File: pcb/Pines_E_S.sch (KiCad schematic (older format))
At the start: 27 parts, among them P1 CONN_01X04, P10 CONN_01X02, P11 CONN_01X02, P12 CONN_01X02, P13 CONN_01X02, P14 USB_MINI, P15 CONN_01X02, P16 CONN_02X03, P2 CONN_01X04, P3 CONN_01X03, P4 CONN_01X03, P5 CONN_01X03, P6 CONN_01X03, P7 CONN_01X03, P8 CONN_01X03, P9 CONN_01X02

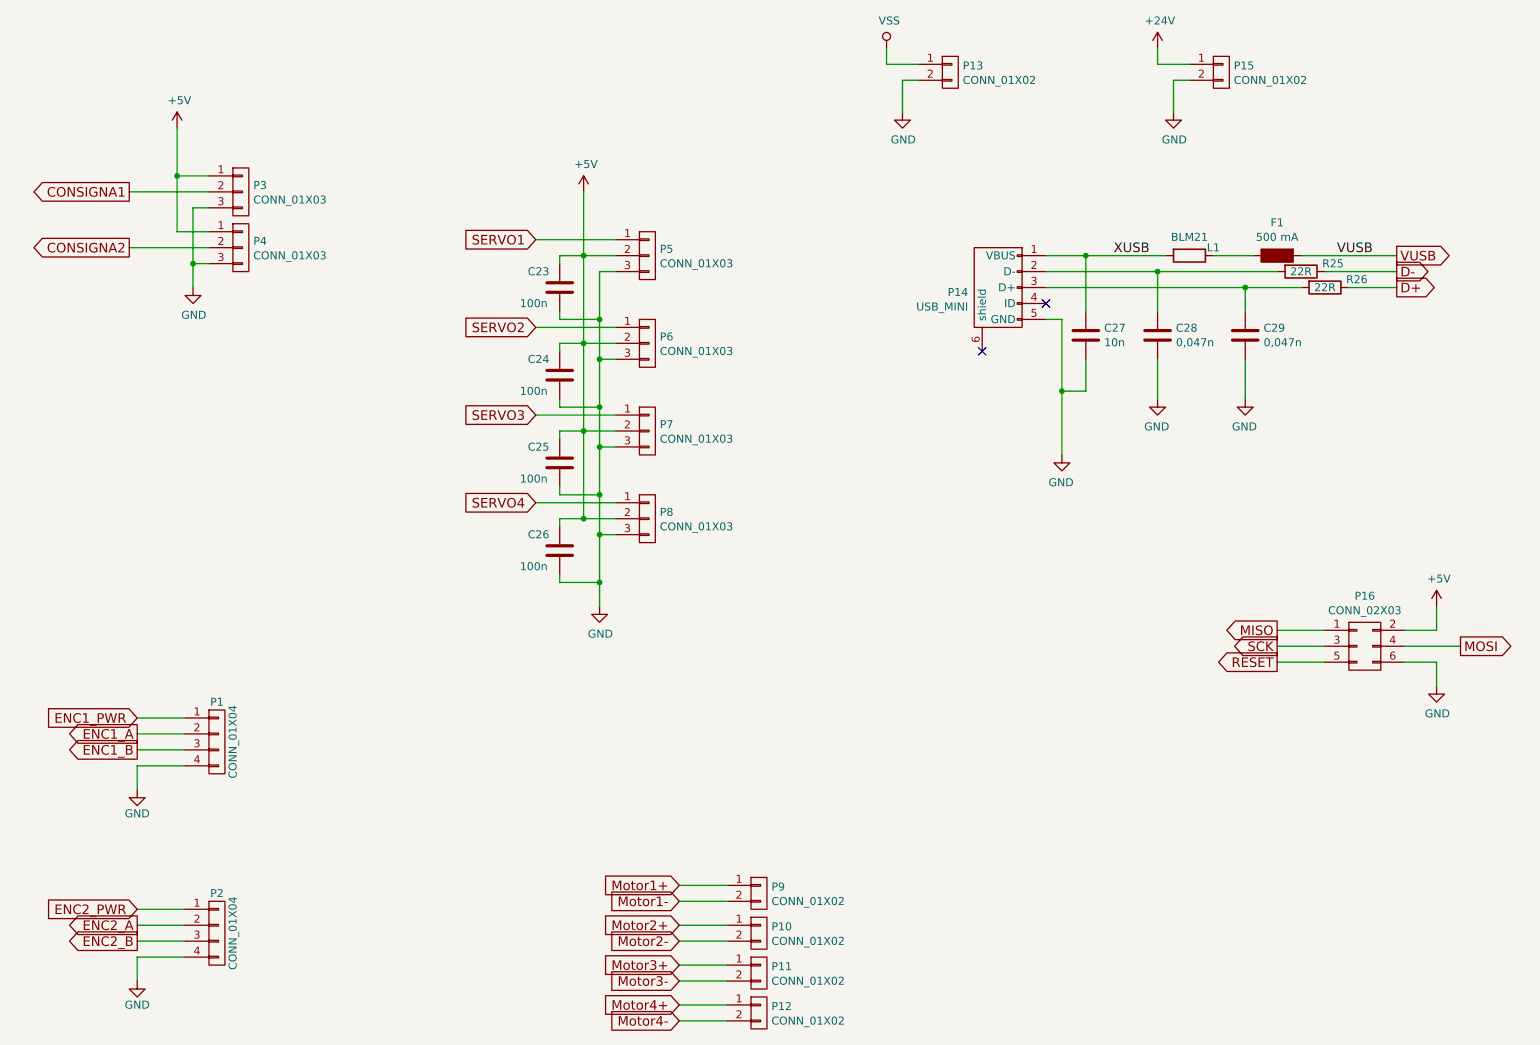
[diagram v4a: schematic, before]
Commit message: añadidas huellas para los borneros
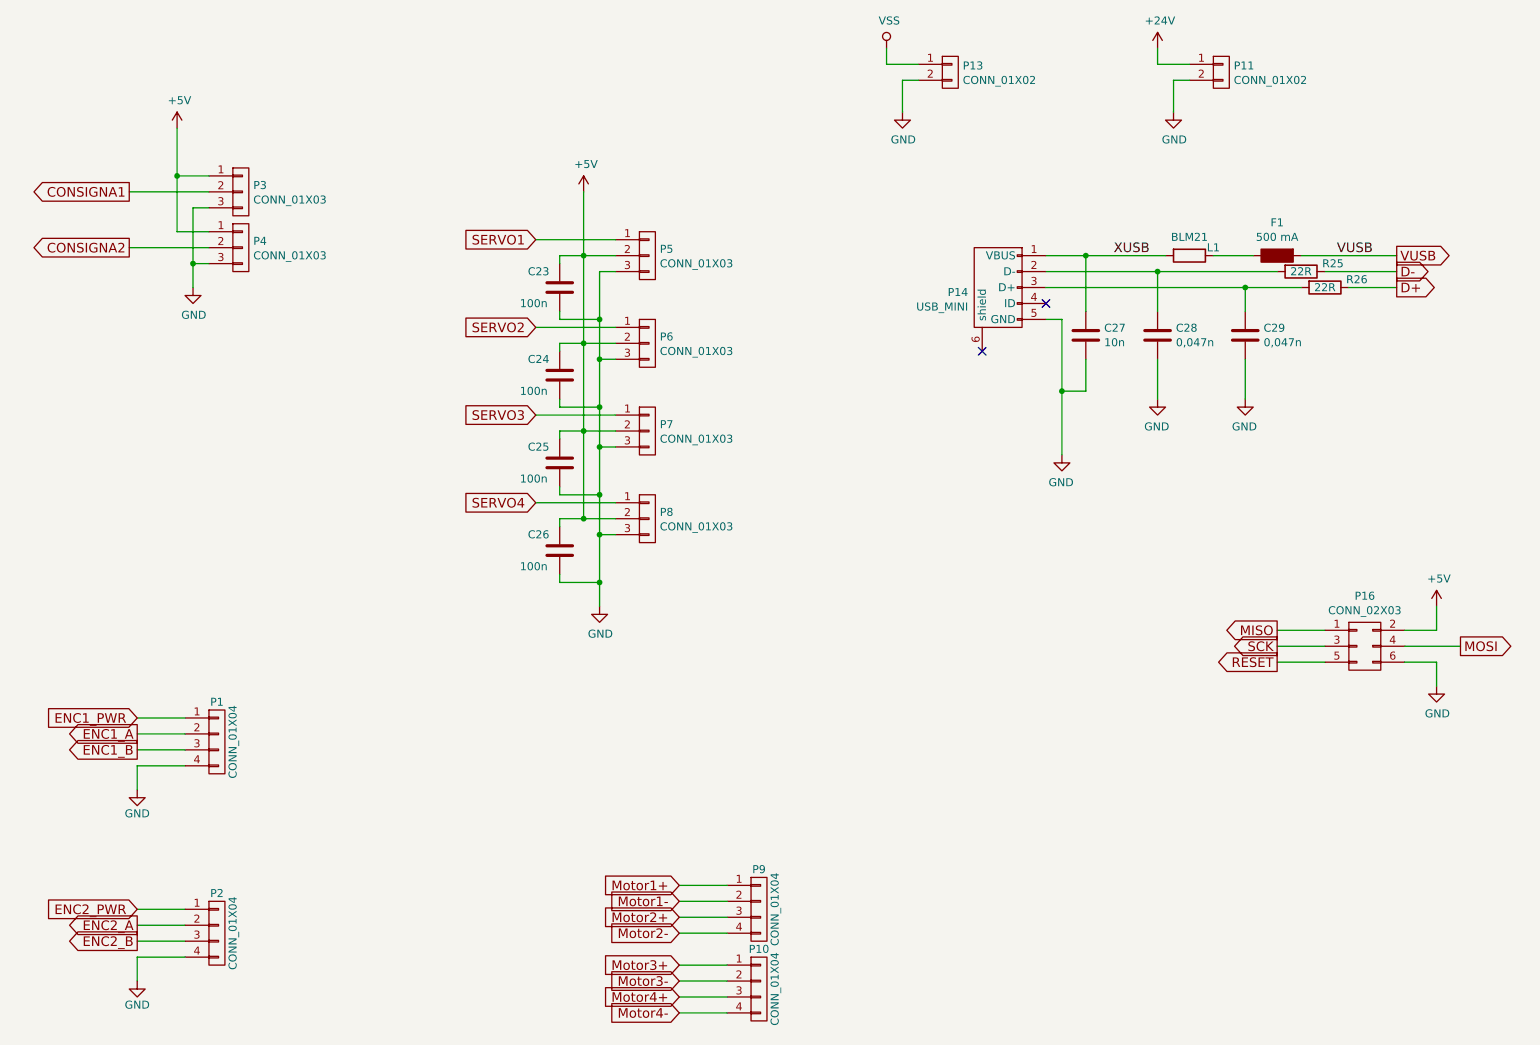
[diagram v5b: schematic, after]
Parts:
- removed P10, P12, P15, P9: CONN_01X02, symbol CONN_01X02
- added P10, P9: CONN_01X04, PhoenixContact:PhoenixContact_MC_1_5x4x3_81, symbol CONN_01X04
- F1: footprint (none) -> Resistencias:R_1812
- L1: footprint (none) -> Capacitors_SMD:C_0805
- P1, P2: footprint (none) -> PhoenixContact:PhoenixContact_MC_1_5x4x3_81; Fabricante (none) -> phoenix contact; Provedor (none) -> rs; Ref (none) -> 1803293 + 1803594; Ref_Proveedor (none) -> 649-0128
- P11, P13: footprint (none) -> PhoenixContact:PhoenixContact_MC_1_5x2x3_81; Fabricante (none) -> phoenix contact; Provedor (none) -> tme; Ref (none) -> 1803277 + 1803578; Ref_Proveedor (none) -> MC1.5/2-G-3.81
- P16: footprint (none) -> Pin_Headers:Pin_Header_Straight_2x03
- P3, P4: footprint (none) -> PhoenixContact:PhoenixContact_MC_1_5x3x3_81; Fabricante (none) -> phoenix contact; Provedor (none) -> tme; Ref (none) -> 1803280 + 1803581; Ref_Proveedor (none) -> MC1.5/3-G-3.81
- P5, P6, P7, P8: footprint (none) -> Pin_Headers:Pin_Header_Straight_1x03
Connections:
- net +24V: now also P11.1 (P1)
- net GND: now also P11.2 (P2)
- net Motor1+: now also P9.1 (P1)
- net Motor1-: now also P9.2 (P2)
- net Motor2+: now also P9.3 (P3)
- net Motor2-: now also P9.4 (P4)
- net Motor3+: now also P10.1 (P1); no longer P11.1 (P1)
- net Motor3-: now also P10.2 (P2); no longer P11.2 (P2)
- net Motor4+: now also P10.3 (P3)
- net Motor4-: now also P10.4 (P4)

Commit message: Colocados todos los componenetes en el area. A revisar
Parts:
- added P12: CONN_01X03, PhoenixContact:PhoenixContact_MC_1_5x3x3_81, symbol CONN_01X03
- added P15: CONN_01X02, PhoenixContact:PhoenixContact_MC_1_5x2x3_81, symbol CONN_01X02
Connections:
- new net DI1: P12.3 (P3)
- new net DI2: P12.2 (P2)
- new net DI3: P12.1 (P1)
- new net DO1: P15.1 (P1)
- new net DO2: P15.2 (P2)
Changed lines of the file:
@@
 	1    0    0    -1
 $EndComp
+$Comp
+L CONN_01X03 P12
+U 1 1 577B1D45
+P 2450 3300
+F 0 "P12" H 2528 3341 50  0000 L CNN
+F 1 "CONN_01X03" H 2528 3250 50  0000 L CNN
+F 2 "PhoenixContact:PhoenixContact_MC_1_5x3x3_81" H 2450 3300 50  0001 C CNN
+F 3 "" H 2450 3300 50  0000 C CNN
+F 4 "phoenix contact" H 1000 3350 60  0001 C CNN "Fabricante"
+F 5 "1803280 + 1803581" H 1000 3350 60  0001 C CNN "Ref"
+F 6 "~" H 1000 3350 60  0001 C CNN "Potencia"
+F 7 "~" H 1000 3350 60  0001 C CNN "Tolerancia"
+F 8 "tme" H 1000 3350 60  0001 C CNN "Provedor"
+F 9 "MC1.5/3-G-3.81" H 1000 3350 60  0001 C CNN "Ref_Proveedor"
+	1    2450 3300
+	1    0    0    -1
+$EndComp
+Text GLabel 1750 3200 0    60   Output ~ 0
+DI3
+Text GLabel 1750 3300 0    60   Output ~ 0
+DI2
+Text GLabel 1750 3400 0    60   Output ~ 0
+DI1
+Wire Wire Line
+	1750 3200 2250 3200
+Wire Wire Line
+	2250 3300 1750 3300
+Wire Wire Line
+	1750 3400 2250 3400
+$Comp
+L CONN_01X02 P15
+U 1 1 577B226D
+P 2450 3750
+F 0 "P15" H 2528 3791 50  0000 L CNN
+F 1 "CONN_01X02" H 2528 3700 50  0000 L CNN
+F 2 "PhoenixContact:PhoenixContact_MC_1_5x2x3_81" H 2450 3750 50  0001 C CNN
+F 3 "" H 2450 3750 50  0000 C CNN
+F 4 "phoenix contact" H -2850 5950 60  0001 C CNN "Fabricante"
+F 5 "1803277 + 1803578" H -2850 5950 60  0001 C CNN "Ref"
+F 6 "~" H -2850 5950 60  0001 C CNN "Potencia"
+F 7 "~" H -2850 5950 60  0001 C CNN "Tolerancia"
+F 8 "tme" H -2850 5950 60  0001 C CNN "Provedor"
+F 9 "MC1.5/2-G-3.81" H -2850 5950 60  0001 C CNN "Ref_Proveedor"
+	1    2450 3750
+	1    0    0    -1
+$EndComp
+Text GLabel 1750 3700 0    60   Input ~ 0
+DO1
+Text GLabel 1750 3800 0    60   Input ~ 0
+DO2
+Wire Wire Line
+	1750 3700 2250 3700
+Wire Wire Line
+	2250 3800 1750 3800
 $EndSCHEMATC

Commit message: añadida huella para choke alimentacion
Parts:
- P1, P2: footprint PhoenixContact:PhoenixContact_MC_1_5x4x3_81 -> PhoenixContact:PhoenixContact_MPT_0,5_4-2,54
- P10, P9: footprint PhoenixContact:PhoenixContact_MC_1_5x4x3_81 -> PhoenixContact:PhoenixContact_mkdsn_4_5.08
- P11, P13: footprint PhoenixContact:PhoenixContact_MC_1_5x2x3_81 -> PhoenixContact:PhoenixContact_mkdsn_2_5.08
- P12, P3, P4: footprint PhoenixContact:PhoenixContact_MC_1_5x3x3_81 -> PhoenixContact:PhoenixContact_MPT_0,5_3-2,54
- P15: footprint PhoenixContact:PhoenixContact_MC_1_5x2x3_81 -> PhoenixContact:PhoenixContact_MPT_0,5_3-2,54
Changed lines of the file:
@@
 F 0 "P3" H 2528 1991 50  0000 L CNN
 F 1 "CONN_01X03" H 2528 1900 50  0000 L CNN
-F 2 "PhoenixContact:PhoenixContact_MC_1_5x3x3_81" H 2450 1950 50  0001 C CNN
+F 2 "PhoenixContact:PhoenixContact_MPT_0,5_3-2,54" H 2450 1950 50  0001 C CNN
 F 3 "" H 2450 1950 50  0000 C CNN
 F 4 "phoenix contact" H 1000 2350 60  0001 C CNN "Fabricante"
@@
 F 0 "P4" H 2528 2341 50  0000 L CNN
 F 1 "CONN_01X03" H 2528 2250 50  0000 L CNN
-F 2 "PhoenixContact:PhoenixContact_MC_1_5x3x3_81" H 2450 2300 50  0001 C CNN
+F 2 "PhoenixContact:PhoenixContact_MPT_0,5_3-2,54" H 2450 2300 50  0001 C CNN
 F 3 "" H 2450 2300 50  0000 C CNN
 F 4 "phoenix contact" H 1000 2350 60  0001 C CNN "Fabricante"
@@
 F 0 "P13" H 6978 1241 50  0000 L CNN
 F 1 "CONN_01X02" H 6978 1150 50  0000 L CNN
-F 2 "PhoenixContact:PhoenixContact_MC_1_5x2x3_81" H 6900 1200 50  0001 C CNN
+F 2 "PhoenixContact:PhoenixContact_mkdsn_2_5.08" H 6900 1200 50  0001 C CNN
 F 3 "" H 6900 1200 50  0000 C CNN
 F 4 "phoenix contact" H 1600 3400 60  0001 C CNN "Fabricante"
@@
 F 0 "P1" H 2300 5650 50  0000 C CNN
 F 1 "CONN_01X04" V 2400 5400 50  0000 C CNN
-F 2 "PhoenixContact:PhoenixContact_MC_1_5x4x3_81" H 2300 5400 50  0001 C CNN
+F 2 "PhoenixContact:PhoenixContact_MPT_0,5_4-2,54" H 2300 5400 50  0001 C CNN
 F 3 "" H 2300 5400 50  0000 C CNN
 F 4 "phoenix contact" H 1450 2700 60  0001 C CNN "Fabricante"
@@
 F 0 "P2" H 2300 6850 50  0000 C CNN
 F 1 "CONN_01X04" V 2400 6600 50  0000 C CNN
-F 2 "PhoenixContact:PhoenixContact_MC_1_5x4x3_81" H 2300 6600 50  0001 C CNN
+F 2 "PhoenixContact:PhoenixContact_MPT_0,5_4-2,54" H 2300 6600 50  0001 C CNN
 F 3 "" H 2300 6600 50  0000 C CNN
 F 4 "phoenix contact" H 1450 2700 60  0001 C CNN "Fabricante"
@@
 F 0 "P9" H 5700 6700 50  0000 C CNN
 F 1 "CONN_01X04" V 5800 6450 50  0000 C CNN
-F 2 "PhoenixContact:PhoenixContact_MC_1_5x4x3_81" H 5700 6450 50  0001 C CNN
+F 2 "PhoenixContact:PhoenixContact_mkdsn_4_5.08" H 5700 6450 50  0001 C CNN
 F 3 "" H 5700 6450 50  0000 C CNN
 F 4 "phoenix contact" H 1450 2700 60  0001 C CNN "Fabricante"
@@
 F 0 "P10" H 5700 7200 50  0000 C CNN
 F 1 "CONN_01X04" V 5800 6950 50  0000 C CNN
-F 2 "PhoenixContact:PhoenixContact_MC_1_5x4x3_81" H 5700 6950 50  0001 C CNN
+F 2 "PhoenixContact:PhoenixContact_mkdsn_4_5.08" H 5700 6950 50  0001 C CNN
 F 3 "" H 5700 6950 50  0000 C CNN
 F 4 "phoenix contact" H 1450 2700 60  0001 C CNN "Fabricante"
@@
 F 0 "P11" H 8678 1241 50  0000 L CNN
 F 1 "CONN_01X02" H 8678 1150 50  0000 L CNN
-F 2 "PhoenixContact:PhoenixContact_MC_1_5x2x3_81" H 8600 1200 50  0001 C CNN
+F 2 "PhoenixContact:PhoenixContact_mkdsn_2_5.08" H 8600 1200 50  0001 C CNN
 F 3 "" H 8600 1200 50  0000 C CNN
 F 4 "phoenix contact" H 1600 3400 60  0001 C CNN "Fabricante"
@@
 F 0 "P12" H 2528 3341 50  0000 L CNN
 F 1 "CONN_01X03" H 2528 3250 50  0000 L CNN
-F 2 "PhoenixContact:PhoenixContact_MC_1_5x3x3_81" H 2450 3300 50  0001 C CNN
+F 2 "PhoenixContact:PhoenixContact_MPT_0,5_3-2,54" H 2450 3300 50  0001 C CNN
 F 3 "" H 2450 3300 50  0000 C CNN
 F 4 "phoenix contact" H 1000 3350 60  0001 C CNN "Fabricante"
@@
 F 0 "P15" H 2528 3791 50  0000 L CNN
 F 1 "CONN_01X02" H 2528 3700 50  0000 L CNN
-F 2 "PhoenixContact:PhoenixContact_MC_1_5x2x3_81" H 2450 3750 50  0001 C CNN
+F 2 "PhoenixContact:PhoenixContact_MPT_0,5_3-2,54" H 2450 3750 50  0001 C CNN
 F 3 "" H 2450 3750 50  0000 C CNN
 F 4 "phoenix contact" H -2850 5950 60  0001 C CNN "Fabricante"
